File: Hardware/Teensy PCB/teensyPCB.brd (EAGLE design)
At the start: 100 x 50 mm, 31 parts, among them U2 USD-SOCKETNEW

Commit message: layout
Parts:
- moved LIN_ARRAY 6.25 mm to (45.0, 3.75)
- moved J2 1.25 mm to (96.2, 15.0)
- moved U$1 1.25 mm to (50.0, 31.2)
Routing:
- net 5V: track 0.00 -> 172.8 mm, vias 0 -> 1
- net 3.3V: track 0.00 -> 155.6 mm, vias 0 -> 2
- net N$2: track 0.00 -> 76.4 mm, vias 0 -> 1
- net SCL1: track 0.00 -> 66.4 mm, vias 0 -> 1
- net N$4: track 0.00 -> 65.3 mm, vias 0 -> 2
- net SDA1: track 0.00 -> 64.5 mm, vias 0 -> 1
- net SDA0: track 0.00 -> 59.6 mm
- net CS: track 0.00 -> 58.8 mm
- net N$9: track 0.00 -> 51.5 mm, vias 0 -> 2
- net MOSI: track 0.00 -> 47.7 mm, vias 0 -> 1
- net SCL0: track 0.00 -> 46.4 mm, vias 0 -> 2
- net N$10: track 0.00 -> 43.9 mm, vias 0 -> 2
- net MISO: track 0.00 -> 37.3 mm, vias 0 -> 1
- net VBAT: track 0.00 -> 29.3 mm
- net AOUT: track 0.00 -> 26.2 mm, vias 0 -> 1
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- added copper zone on layer 1, net GND
- added copper zone on layer 16, net GND

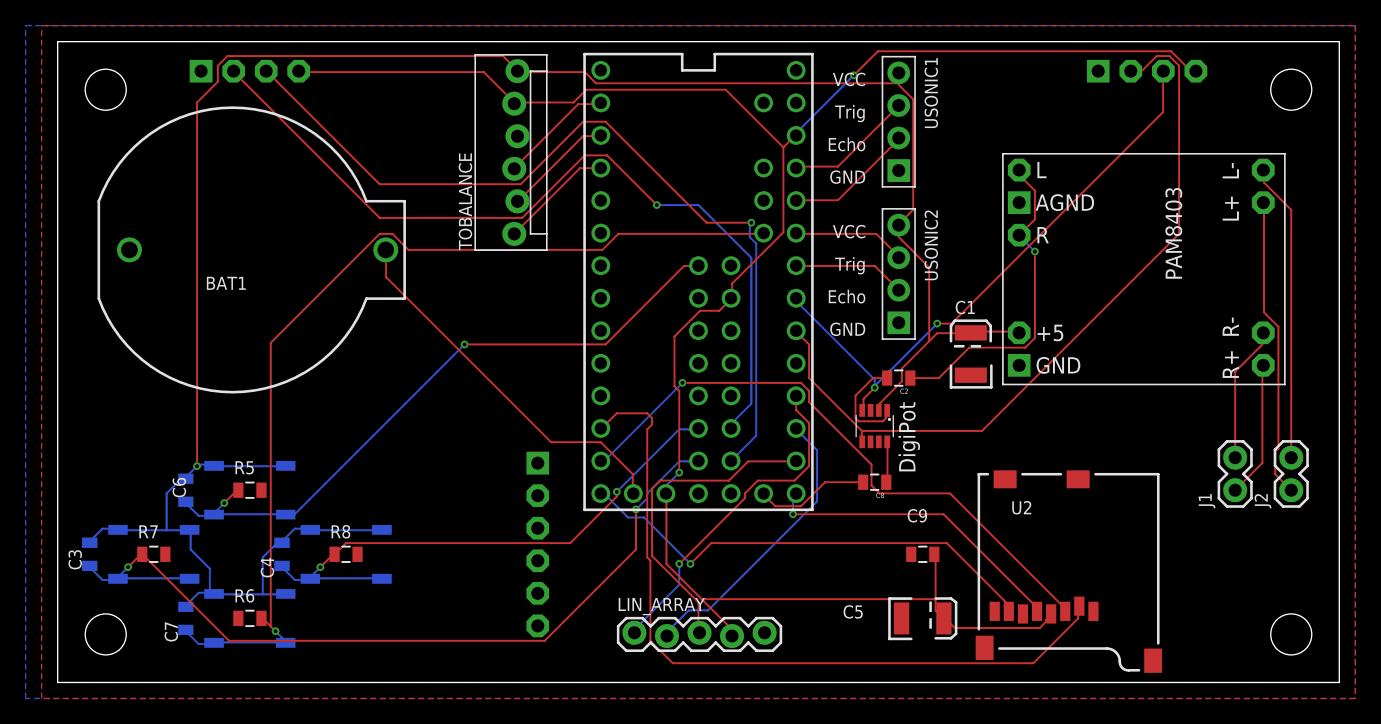
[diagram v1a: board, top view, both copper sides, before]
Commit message: fixed HC-05 text and added leds
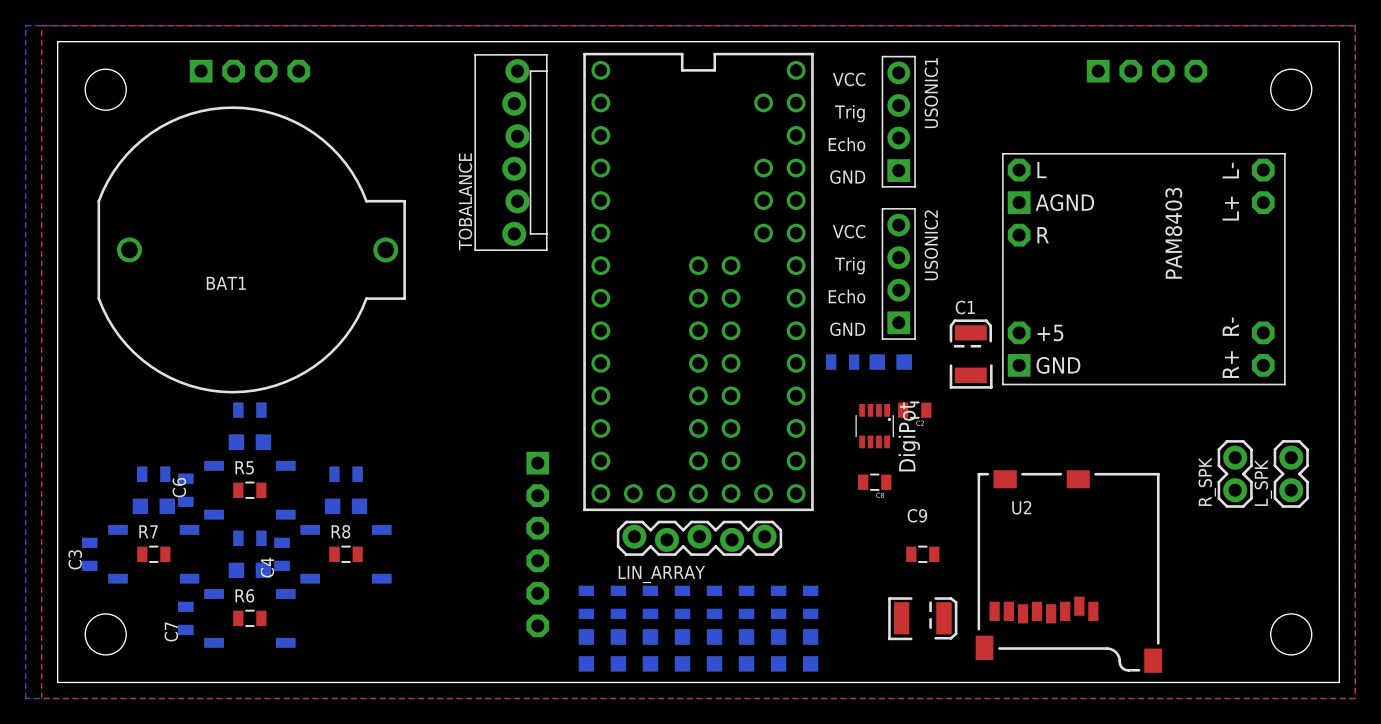
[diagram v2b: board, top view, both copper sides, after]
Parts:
- added LED1, LED10, LED11, LED12, LED13, LED2, LED3, LED4, LED5, LED6, LED7, LED8, LED9: (no value), adafruit:CHIP-LED0805
- added R1, R10, R11, R12, R13, R14, R15, R16, R17, R2, R3, R4, R9: 1k, SparkFun-Resistors:0805
- S3: value LEFT -> RIGHT
- S4: value RIGHT -> LEFT
- moved LIN_ARRAY 7.50 mm to (45.0, 11.2)
- moved C2 2.80 mm to (66.9, 21.2)
- renumbered J1 to R_SPK, J2 to L_SPK
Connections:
- removed net AGND: U$1.AGND
- removed net AREF: U$1.AREF
- removed net SW: U$1.A13
- new net BLUETOOTH_KEY: J_BT_BOARD_1.KEY, U$1.24
- new net BLUETOOTH_RX: J_BT_BOARD_1.RX, U$1.7
- new net BLUETOOTH_TX: J_BT_BOARD_1.TX, U$1.8
- new net CARD_DETECT: U2.CD1, U2.CD2
- new net LED1: R1.2, U$1.3
- new net LED10: R14.2, U$1.32
- new net LED11: R15.2, U$1.31
- new net LED12: R16.2, U$1.26
- new net LED13: R17.2, U$1.25
- new net LED2: R2.2, U$1.4
- new net LED3: R3.2, U$1.5
- new net LED4: R4.2, U$1.6
- new net LED5: R9.2, U$1.9
- new net LED6: R10.2, U$1.17/A3
- new net LED7: R11.2, U$1.A13
- new net LED8: R12.2, U$1.A10
- new net LED9: R13.2, U$1.33
- new net N$11: LED1.A, R1.1
- new net N$12: LED2.A, R2.1
- new net N$13: LED3.A, R3.1
- new net N$14: LED4.A, R4.1
- new net N$15: LED5.A, R9.1
- new net N$16: LED6.A, R10.1
- new net N$17: LED7.A, R11.1
- new net N$18: LED8.A, R12.1
- new net N$19: LED9.A, R13.1
- new net N$20: LED10.A, R14.1
- new net N$21: LED11.A, R15.1
- new net N$22: LED12.A, R16.1
- new net N$23: LED13.A, R17.1
- net 3.3V: now also U$1.AREF
- net 5V: now also J_BT_BOARD_1.VCC
- net GND: now also J_BT_BOARD_1.GND, LED1.C, LED10.C, LED11.C, LED12.C, LED13.C, LED2.C, LED3.C, LED4.C, LED5.C, LED6.C, LED7.C, LED8.C, LED9.C, U$1.AGND, U2.GND1, U2.GND3
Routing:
- net 5V: track 172.8 -> 0.00 mm, vias 1 -> 0
- net 3.3V: track 155.6 -> 0.00 mm, vias 2 -> 0
- net N$2: track 76.4 -> 0.00 mm, vias 1 -> 0
- net SCL1: track 66.4 -> 0.00 mm, vias 1 -> 0
- net N$4: track 65.3 -> 0.00 mm, vias 2 -> 0
- net SDA1: track 64.5 -> 0.00 mm, vias 1 -> 0
- net SDA0: track 59.6 -> 0.00 mm
- net CS: track 58.8 -> 0.00 mm
- net N$9: track 51.5 -> 0.00 mm, vias 2 -> 0
- net MOSI: track 47.7 -> 0.00 mm, vias 1 -> 0
- net SCL0: track 46.4 -> 0.00 mm, vias 2 -> 0
- net N$10: track 43.9 -> 0.00 mm, vias 2 -> 0
- net MISO: track 37.3 -> 0.00 mm, vias 1 -> 0
- net VBAT: track 29.3 -> 0.00 mm
- net AOUT: track 26.2 -> 0.00 mm, vias 1 -> 0
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
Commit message: fixed 5V connected to buttons
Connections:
- net 3.3V: now also C3.1, C4.1, C6.1, C7.1, S1.1, S1.2, S2.1, S2.2, S3.1, S3.2, S4.1, S4.2
- net 5V: no longer C3.1, C4.1, C6.1, C7.1, S1.1, S1.2, S2.1, S2.2, S3.1, S3.2, S4.1, S4.2
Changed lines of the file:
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@@
 <contactref element="C9" pad="1"/>
 <contactref element="U$1" pad="AREF"/>
+<contactref element="S1" pad="1"/>
+<contactref element="S2" pad="1"/>
+<contactref element="S2" pad="2"/>
+<contactref element="C6" pad="1"/>
+<contactref element="C7" pad="1"/>
+<contactref element="S1" pad="2"/>
+<contactref element="S3" pad="2"/>
+<contactref element="S4" pad="2"/>
+<contactref element="S3" pad="1"/>
+<contactref element="C3" pad="1"/>
+<contactref element="C4" pad="1"/>
+<contactref element="S4" pad="1"/>
 <wire x1="57.62" y1="42.68" x2="88.81" y2="47.7" width="0" layer="19" extent="1-1"/>
 <wire x1="55.08" y1="40.14" x2="57.62" y2="42.68" width="0" layer="19" extent="1-1"/>
@@
 <wire x1="35.625" y1="45.16" x2="55.08" y2="40.14" width="0" layer="19" extent="1-1"/>
 <wire x1="18.81" y1="47.7" x2="35.625" y2="45.16" width="0" layer="19" extent="1-1"/>
-</signal>
-<signal name="5V" class="1">
-<contactref element="TOBALANCE" pad="6"/>
-<contactref element="USONIC2" pad="VCC"/>
-<contactref element="USONIC1" pad="VCC"/>
-<contactref element="U$5" pad="VDD"/>
-<contactref element="S1" pad="1"/>
-<contactref element="S1" pad="2"/>
-<contactref element="S2" pad="2"/>
-<contactref element="S2" pad="1"/>
-<contactref element="C1" pad="A"/>
-<contactref element="S3" pad="2"/>
-<contactref element="S3" pad="1"/>
-<contactref element="S4" pad="2"/>
-<contactref element="S4" pad="1"/>
-<contactref element="U$4" pad="+5V"/>
-<contactref element="C3" pad="1"/>
-<contactref element="C4" pad="1"/>
-<contactref element="C6" pad="1"/>
-<contactref element="C7" pad="1"/>
-<contactref element="J_BT_BOARD_1" pad="VCC"/>
-<wire x1="65.625" y1="35.685" x2="65.625" y2="47.56" width="0" layer="19" extent="1-1"/>
-<wire x1="71.25" y1="27.275" x2="65.625" y2="35.685" width="0" layer="19" extent="1-1"/>
-<wire x1="75.02" y1="27.28" x2="71.25" y2="27.275" width="0" layer="19" extent="1-1"/>
-<wire x1="64.075" y1="21.225" x2="71.25" y2="27.275" width="0" layer="19" extent="1-1"/>
-<wire x1="37.46" y1="12.035" x2="64.075" y2="21.225" width="0" layer="19" extent="1-1"/>
-<wire x1="25.294" y1="11.905" x2="37.46" y2="12.035" width="0" layer="19" extent="16-16"/>
+<wire x1="25.294" y1="11.905" x2="47.46" y2="14.74" width="0" layer="19" extent="16-16"/>
 <wire x1="19.706" y1="11.905" x2="25.294" y2="11.905" width="0" layer="19" extent="16-16"/>
 <wire x1="17.5" y1="10.9" x2="19.706" y2="11.905" width="0" layer="19" extent="16-16"/>
@@
 <wire x1="4.706" y1="11.905" x2="10.294" y2="11.905" width="0" layer="19" extent="16-16"/>
 <wire x1="2.5" y1="10.9" x2="4.706" y2="11.905" width="0" layer="19" extent="16-16"/>
+</signal>
+<signal name="5V" class="1">
+<contactref element="TOBALANCE" pad="6"/>
+<contactref element="USONIC2" pad="VCC"/>
+<contactref element="USONIC1" pad="VCC"/>
+<contactref element="U$5" pad="VDD"/>
+<contactref element="C1" pad="A"/>
+<contactref element="U$4" pad="+5V"/>
+<contactref element="J_BT_BOARD_1" pad="VCC"/>
+<wire x1="65.625" y1="35.685" x2="65.625" y2="47.56" width="0" layer="19" extent="1-1"/>
+<wire x1="71.25" y1="27.275" x2="65.625" y2="35.685" width="0" layer="19" extent="1-1"/>
+<wire x1="75.02" y1="27.28" x2="71.25" y2="27.275" width="0" layer="19" extent="1-1"/>
+<wire x1="64.075" y1="21.225" x2="71.25" y2="27.275" width="0" layer="19" extent="1-1"/>
+<wire x1="37.46" y1="12.035" x2="64.075" y2="21.225" width="0" layer="19" extent="1-1"/>
 <wire x1="35.879" y1="47.7" x2="65.625" y2="47.56" width="0" layer="19" extent="1-1"/>
 </signal>

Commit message: Changed button pins after @Jeysen found an error
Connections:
- net N$10 renamed BUTTON4
- net N$4 renamed BUTTON3
- removed net N$2: C7.2, R6.2, S2.3, S2.4, U$1.A11
- removed net N$9: C6.2, R5.2, S1.3, S1.4, U$1.A12
- new net BUTTON1: C6.2, R5.2, S1.3, S1.4, U$1.33
- new net BUTTON2: C7.2, R6.2, S2.3, S2.4, U$1.32
- net LED10: no longer U$1.32
- net LED9: no longer U$1.33
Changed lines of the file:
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@@
 <wire x1="65.975" y1="21.25" x2="64.725" y2="21.225" width="0" layer="19" extent="1-1"/>
 </signal>
-<signal name="N$9">
+<signal name="BUTTON1">
 <contactref element="S1" pad="3"/>
 <contactref element="S1" pad="4"/>
 <contactref element="R5" pad="2"/>
-<contactref element="U$1" pad="A12"/>
 <contactref element="C6" pad="2"/>
-<wire x1="17.794" y1="13.095" x2="50" y2="32.52" width="0" layer="19" extent="16-16"/>
+<contactref element="U$1" pad="33"/>
+<wire x1="17.794" y1="13.095" x2="52.54" y2="27.44" width="0" layer="19" extent="16-16"/>
 <wire x1="14.1" y1="15" x2="17.794" y2="13.095" width="0" layer="19" extent="1-16"/>
 <wire x1="12.206" y1="13.095" x2="14.1" y2="15" width="0" layer="19" extent="1-16"/>
 <wire x1="10" y1="14.1" x2="12.206" y2="13.095" width="0" layer="19" extent="16-16"/>
 </signal>
-<signal name="N$2">
+<signal name="BUTTON2">
 <contactref element="S2" pad="4"/>
 <contactref element="S2" pad="3"/>
 <contactref element="R6" pad="2"/>
-<contactref element="U$1" pad="A11"/>
 <contactref element="C7" pad="2"/>
-<wire x1="17.794" y1="3.095" x2="55.08" y2="35.06" width="0" layer="19" extent="16-16"/>
+<contactref element="U$1" pad="32"/>
+<wire x1="17.794" y1="3.095" x2="52.54" y2="24.9" width="0" layer="19" extent="16-16"/>
 <wire x1="15.9" y1="5" x2="17.794" y2="3.095" width="0" layer="19" extent="1-16"/>
 <wire x1="12.206" y1="3.095" x2="15.9" y2="5" width="0" layer="19" extent="1-16"/>
@@
 <contactref element="U$1" pad="VUSB"/>
 </signal>
-<signal name="N$4">
+<signal name="BUTTON3">
 <contactref element="S3" pad="4"/>
 <contactref element="S3" pad="3"/>
@@
 <wire x1="2.5" y1="9.1" x2="4.706" y2="8.095" width="0" layer="19" extent="16-16"/>
 </signal>
-<signal name="N$10">
+<signal name="BUTTON4">
 <contactref element="S4" pad="4"/>
 <contactref element="S4" pad="3"/>
@@
 <signal name="LED9">
 <contactref element="R13" pad="2"/>
-<contactref element="U$1" pad="33"/>
-<wire x1="53.75" y1="7.15" x2="52.54" y2="27.44" width="0" layer="19" extent="16-16"/>
 </signal>
 <signal name="LED10">
 <contactref element="R14" pad="2"/>
-<contactref element="U$1" pad="32"/>
-<wire x1="48.75" y1="7.15" x2="52.54" y2="24.9" width="0" layer="19" extent="16-16"/>
 </signal>
 <signal name="LED11">

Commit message: Supplemental
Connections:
- net LED10: now also U$1.A11
- net LED9: now also U$1.A12
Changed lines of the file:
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@@
 <signal name="LED9">
 <contactref element="R13" pad="2"/>
+<contactref element="U$1" pad="A12"/>
+<wire x1="53.75" y1="7.15" x2="50" y2="32.52" width="0" layer="19" extent="16-16"/>
 </signal>
 <signal name="LED10">
 <contactref element="R14" pad="2"/>
+<contactref element="U$1" pad="A11"/>
+<wire x1="48.75" y1="7.15" x2="55.08" y2="35.06" width="0" layer="19" extent="16-16"/>
 </signal>
 <signal name="LED11">

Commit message: PCB finalized
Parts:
- removed C8: 10uF, SparkFun-Capacitors:0805
- removed U2: USD-SOCKETNEW, SparkFun-Connectors:MICRO-SD-SOCKET-PP
- added C10: 10uF, SparkFun-Capacitors:EIA3528
- added MICRO_SD: USD-SOCKETNEW, SparkFun-Connectors:MICRO-SD-SOCKET-PP
- moved LED6 22.6 mm to (60.0, 3.00), turned to 180 degrees
- moved L_SPK 22.2 mm to (96.9, 37.2)
- moved R10 18.3 mm to (60.0, 6.75), turned to 90 degrees
- moved J_BT_BOARD_1 17.1 mm to (38.5, 18.9), flipped to the top, turned to 180 degrees
- moved TOBALANCE 13.2 mm to (35.0, 21.8)
- moved R_SPK 10.8 mm to (97.0, 24.5)
- moved U$5 3.82 mm to (63.0, 23.8)
- moved C1 2.01 mm to (69.3, 26.3)
- moved U$4 1.91 mm to (71.8, 41.2)
- moved LED10 1.35 mm to (47.5, 3.00)
- moved LED11 1.35 mm to (50.0, 3.00)
- moved LED12 1.35 mm to (42.5, 3.00)
- moved LED13 1.35 mm to (45.0, 3.00)
- moved LED5 1.35 mm to (40.0, 3.00)
- moved LED7 1.35 mm to (55.0, 3.00)
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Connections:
- removed net N$3: C8.1, U$5.A
- new net N$2: C10.A, U$5.A
- net 3.3V: now also MICRO_SD.4; no longer U2.4
- net CARD_DETECT: now also MICRO_SD.CD1, MICRO_SD.CD2; no longer U2.CD1, U2.CD2
- net CS: now also MICRO_SD.2; no longer U2.2
- net DAC: now also C10.C; no longer C8.2
- net GND: now also MICRO_SD.6, MICRO_SD.GND1, MICRO_SD.GND3; no longer U2.6, U2.GND1, U2.GND3
- net MISO: now also MICRO_SD.7; no longer U2.7
- net MOSI: now also MICRO_SD.3; no longer U2.3
- net SCK: now also MICRO_SD.5; no longer U2.5
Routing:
- net 3.3V: track 0.00 -> 261.5 mm, vias 0 -> 3
- net 5V: track 0.00 -> 114.2 mm, vias 0 -> 2
- net SDA1: track 0.00 -> 88.4 mm
- net BUTTON3: track 0.00 -> 75.5 mm, vias 0 -> 2
- net MISO: track 0.00 -> 64.2 mm
- net SCL1: track 0.00 -> 63.6 mm, vias 0 -> 1
- net CS: track 0.00 -> 61.8 mm, vias 0 -> 3
- net BUTTON1: track 0.00 -> 58.5 mm, vias 0 -> 3
- net BUTTON2: track 0.00 -> 57.6 mm, vias 0 -> 2
- net MOSI: track 0.00 -> 55.8 mm, vias 0 -> 3
- net LED4: track 0.00 -> 46.5 mm, vias 0 -> 3
- net BUTTON4: track 0.00 -> 45.5 mm, vias 0 -> 3
- net SCL0: track 0.00 -> 43.6 mm
- net SDA0: track 0.00 -> 43.1 mm, vias 0 -> 1
- net LED10: track 0.00 -> 42.3 mm, vias 0 -> 3
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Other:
- board text added: "Abul Ali Jeysen Raheel Jonathan"
- board text added: "Self-Balancing Robot Face V0.1"
- board text added: "TEAM FOXTROT ELEC3907 WINTER 2016"
